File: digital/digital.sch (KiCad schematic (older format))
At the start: 0 parts

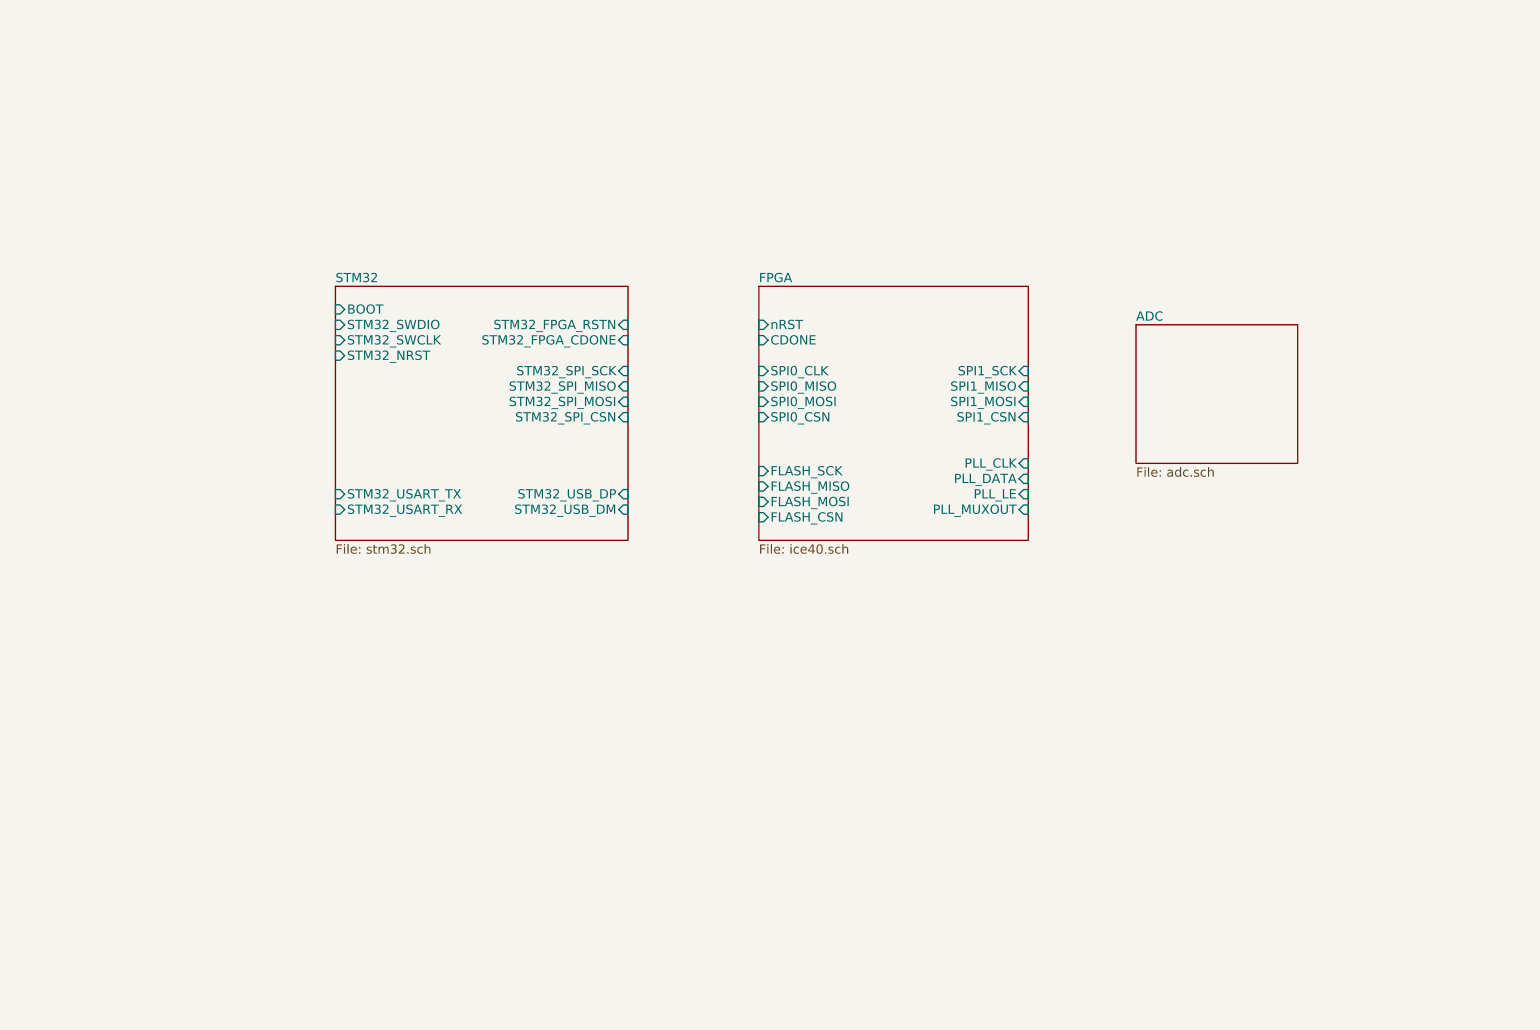
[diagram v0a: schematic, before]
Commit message: Finish schematic TODO footprints
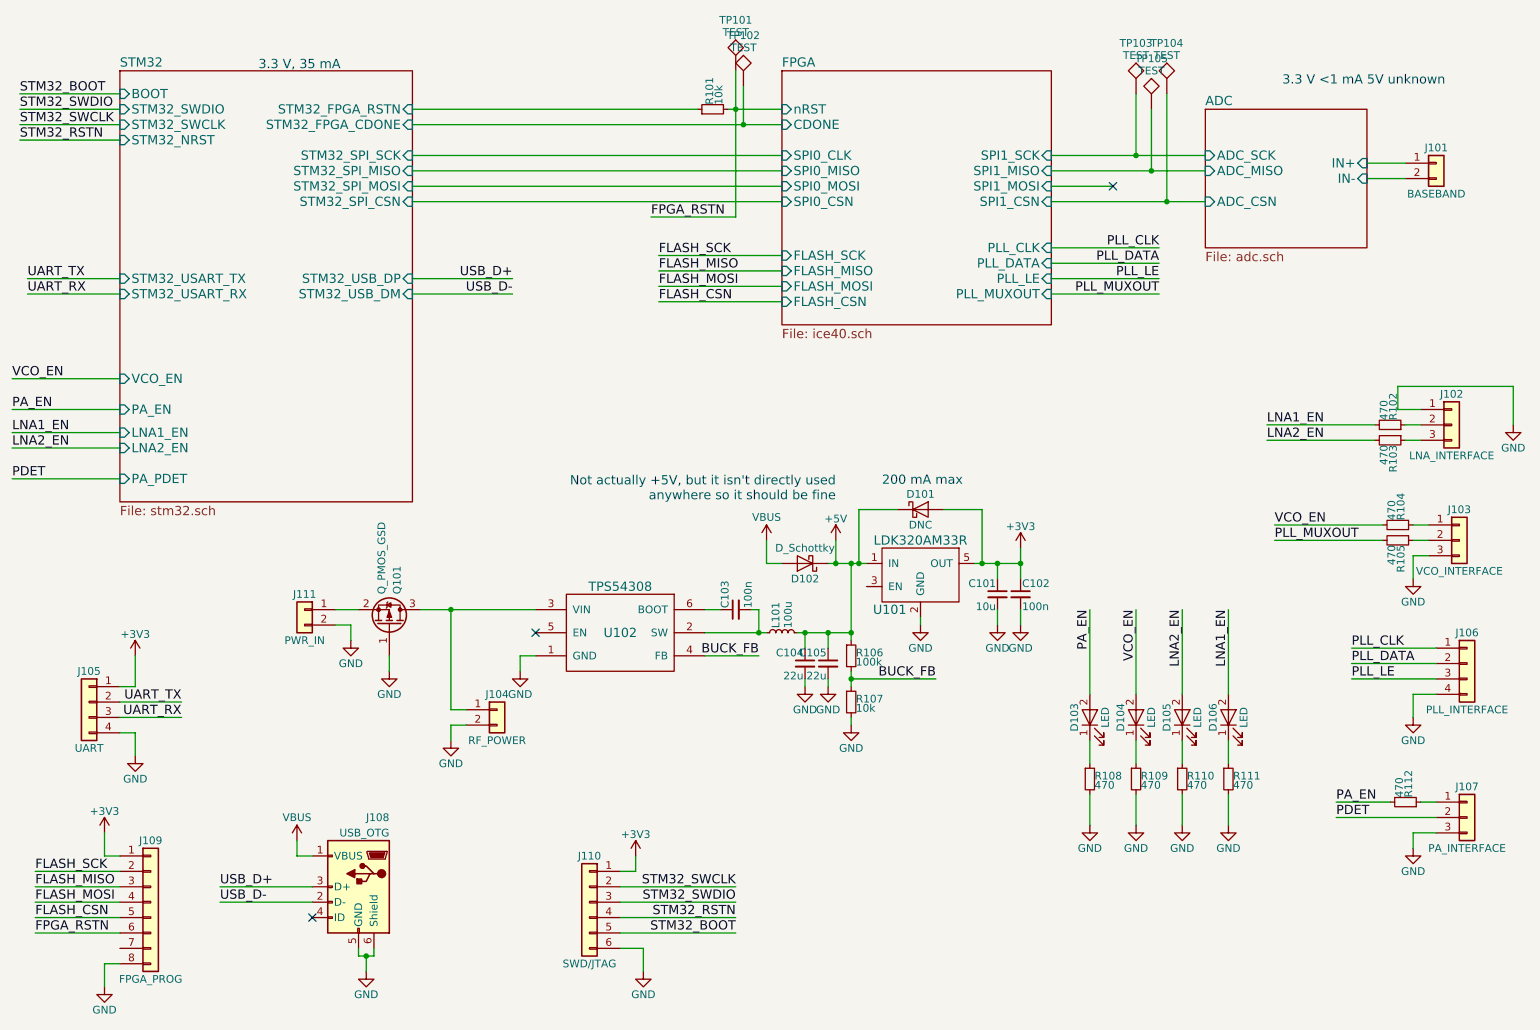
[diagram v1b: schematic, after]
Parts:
- added C101: 10u, symbol C_Small
- added C102, C103: 100n, symbol C_Small
- added C104, C105: 22u, symbol C_Small
- added D101: DNC, symbol D_Schottky
- added D102: D_Schottky, symbol D_Schottky
- added D103, D104, D105, D106: LED, symbol LED
- added J101: BASEBAND, Pin_Headers:Pin_Header_Straight_1x02_Pitch2.54mm, symbol Conn_01x02
- added J102: LNA_INTERFACE, Pin_Headers:Pin_Header_Straight_1x03_Pitch2.54mm, symbol Conn_01x03
- added J103: VCO_INTERFACE, Pin_Headers:Pin_Header_Straight_1x03_Pitch2.54mm, symbol Conn_01x03
- added J104: RF_POWER, Pin_Headers:Pin_Header_Straight_1x02_Pitch2.54mm, symbol Conn_01x02
- added J105: UART, Pin_Headers:Pin_Header_Straight_2x02_Pitch2.54mm, symbol Conn_01x04
- added J106: PLL_INTERFACE, Pin_Headers:Pin_Header_Straight_2x02_Pitch2.54mm, symbol Conn_01x04
- added J107: PA_INTERFACE, Pin_Headers:Pin_Header_Straight_1x03_Pitch2.54mm, symbol Conn_01x03
- added J108: USB_OTG, symbol USB_OTG
- added J109: FPGA_PROG, Pin_Headers:Pin_Header_Straight_2x04_Pitch2.54mm, symbol Conn_01x08
- added J110: SWD/JTAG, Pin_Headers:Pin_Header_Straight_2x03_Pitch2.54mm, symbol Conn_01x06
- added J111: PWR_IN, Pin_Headers:Pin_Header_Straight_1x02_Pitch2.54mm, symbol Conn_01x02
- added L101: 100u, symbol L_Small
- added Q101: Q_PMOS_GSD, TO_SOT_Packages_SMD:SOT-23, symbol Q_PMOS_GSD
- added R101, R107: 10k, symbol R_Small
- added R102, R103, R104, R105, R108, R109, R110, R111, R112: 470, symbol R_Small
- added R106: 100k, symbol R_Small
- added TP101, TP102, TP103, TP104, TP105: TEST, Connectors:PINTST, symbol TEST
- added U101: LDK320AM33R, symbol LDK320AM33R
- added U102: TPS54308, symbol TPS54308
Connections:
- net FPGA/CDONE: now also TP102.1
- net STM32/STM32_FPGA_RSTN: now also R101.1
- new net: J103.1 (Pin_1), R104.1
- new net: J103.2 (Pin_2), R105.1
- new net: J107.1 (Pin_1), R112.1
- new net: J102.2 (Pin_2), R102.1
- new net: J102.3 (Pin_3), R103.1
- new net: J104.1 (Pin_1), Q101.3 (D), U102.3 (VIN)
- new net: D103.1 (K), R108.1
- new net: D106.1 (K), R111.1
- new net: D105.1 (K), R110.1
- new net: D104.1 (K), R109.1
- new net: J111.1 (Pin_1), Q101.2 (S)
- new net: C103.2, L101.1, U102.2 (SW)
- new net: C103.1, U102.6 (BOOT)
- new net +3V3: C101.1, C102.1, D101.2 (A), J105.1 (Pin_1), J109.1 (Pin_1), J110.1 (Pin_1), U101.5 (OUT)
- new net +5V: C104.1, C105.1, D101.1 (K), D102.1 (K), L101.2, R106.1, U101.1 (IN)
- new net ADC/ADC_CSN: TP104.1
- new net ADC/ADC_MISO: TP105.1
- new net ADC/ADC_SCK: TP103.1
- new net ADC/IN+: J101.1 (Pin_1)
- new net ADC/IN-: J101.2 (Pin_2)
- new net BUCK_FB: R106.2, R107.1, U102.4 (FB)
- new net FLASH_CSN: J109.5 (Pin_5)
- new net FLASH_MISO: J109.3 (Pin_3)
- new net FLASH_MOSI: J109.4 (Pin_4)
- new net FLASH_SCK: J109.2 (Pin_2)
- new net FPGA_RSTN: J109.6 (Pin_6), R101.2, TP101.1
- new net GND: C101.2, C102.2, C104.2, C105.2, J102.1 (Pin_1), J103.3 (Pin_3), J104.2 (Pin_2), J105.4 (Pin_4), J106.4 (Pin_4), J107.3 (Pin_3), J108.5 (GND), J108.6 (Shield), J109.8 (Pin_8), J110.6 (Pin_6), J111.2 (Pin_2), Q101.1 (G), R107.2, R108.2, R109.2, R110.2, R111.2, U101.2 (GND), U102.1 (GND)
- new net LNA1_EN: D106.2 (A), R102.2
- new net LNA2_EN: D105.2 (A), R103.2
- new net PA_EN: D103.2 (A), R112.2
- new net PDET: J107.2 (Pin_2)
- new net PLL_CLK: J106.1 (Pin_1)
- new net PLL_DATA: J106.2 (Pin_2)
- new net PLL_LE: J106.3 (Pin_3)
- new net PLL_MUXOUT: R105.2
- new net STM32_BOOT: J110.5 (Pin_5)
- new net STM32_RSTN: J110.4 (Pin_4)
- new net STM32_SWCLK: J110.2 (Pin_2)
- new net STM32_SWDIO: J110.3 (Pin_3)
- new net UART_RX: J105.3 (Pin_3)
- new net UART_TX: J105.2 (Pin_2)
- new net USB_D+: J108.3 (D+)
- new net USB_D-: J108.2 (D-)
- new net VBUS: D102.2 (A), J108.1 (VBUS)
- new net VCO_EN: D104.2 (A), R104.2
- no-connect marks 0 -> 3
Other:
- note added: "200 mA max"
- note added: "3.3 V <1 mA 5V unknown"
- note added: "3.3 V, 35 mA"
- note added: "Not actually +5V, but it isn't directly used\nanywhere so it should be fine"

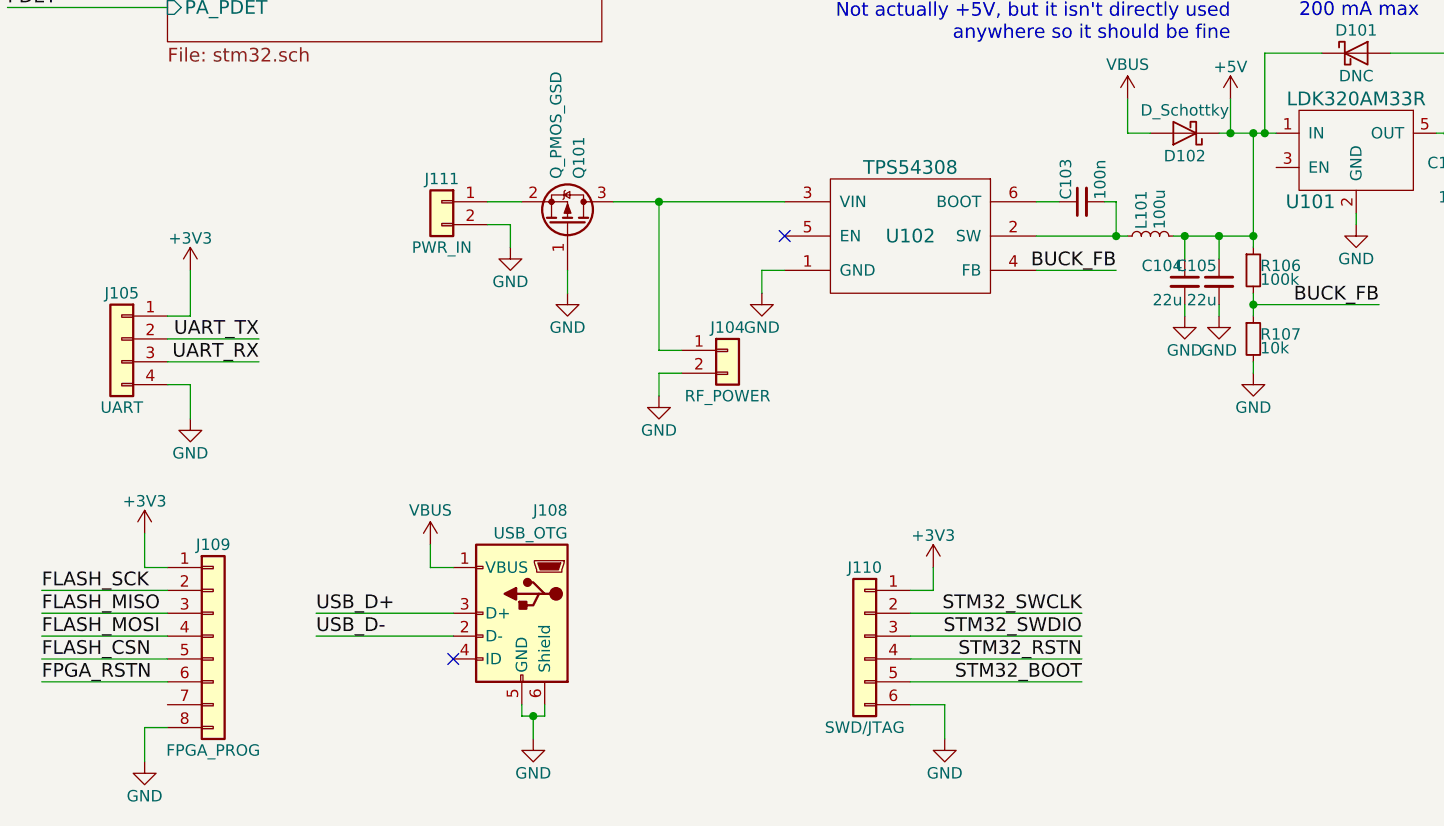
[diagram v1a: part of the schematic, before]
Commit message: Finish schematic and footprinting of digital board
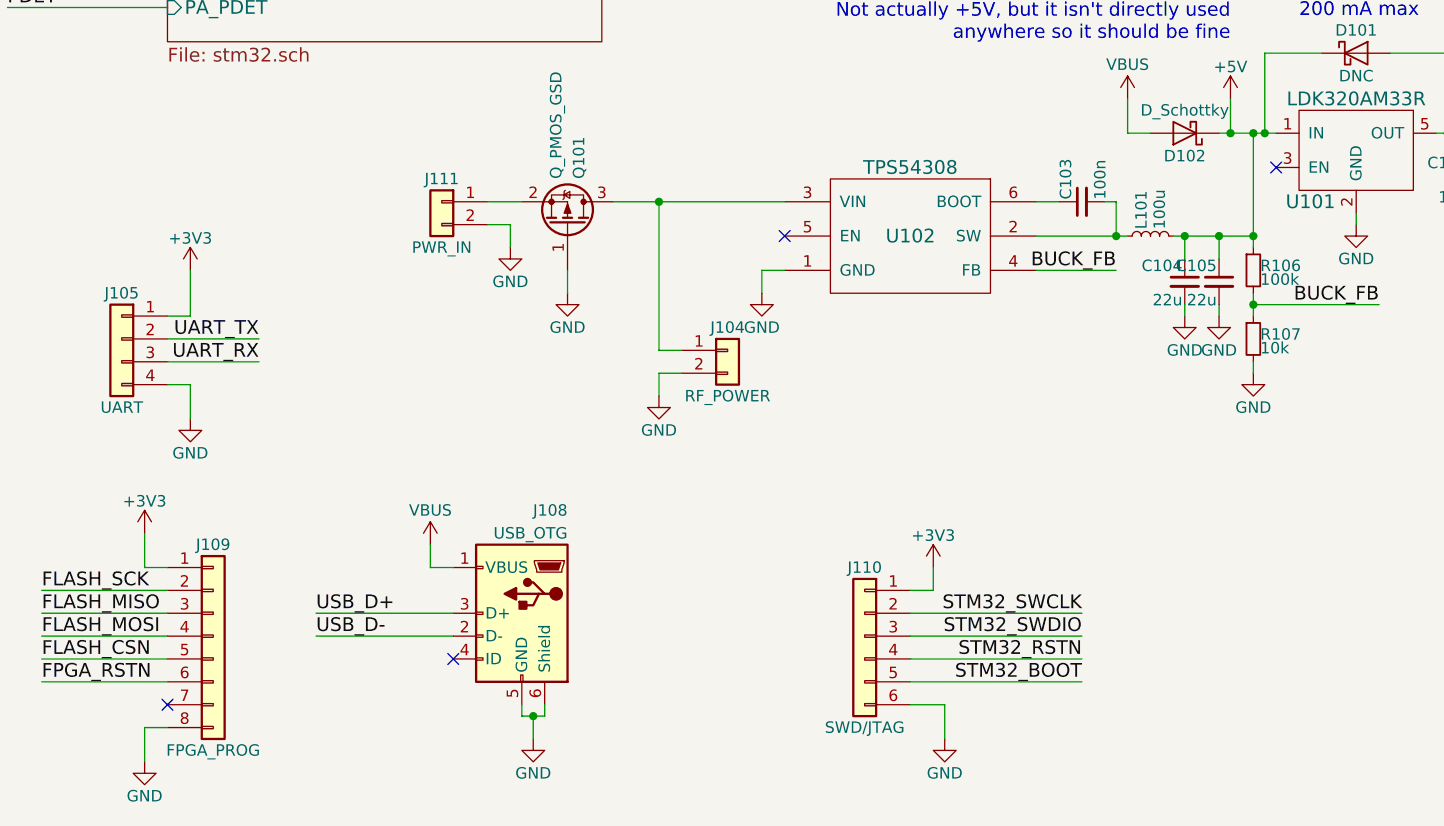
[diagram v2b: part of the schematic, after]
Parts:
- C101: footprint (none) -> Capacitors_SMD:C_0805_HandSoldering
- C102, C103: footprint (none) -> Capacitors_SMD:C_0603_HandSoldering
- C104, C105: footprint (none) -> Capacitors_SMD:C_1210_HandSoldering
- D101, D102: footprint (none) -> digital:Panasonic_Diode-1006
- D103, D104, D105, D106: footprint (none) -> Diodes_SMD:D_0603
- J108: footprint (none) -> digital:10118194
- L101: footprint (none) -> digital:Murata_DG6050C
- R101, R102, R103, R104, R105, R107, R108, R109, R110, R111, R112: footprint (none) -> Resistors_SMD:R_0603_HandSoldering
- R106: footprint (none) -> Resistors_SMD:R_0402
- U101: footprint (none) -> digital:ST_SOT23-5L
- U102: footprint (none) -> digital:TI-SOT-23-6
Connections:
- no-connect marks 3 -> 5

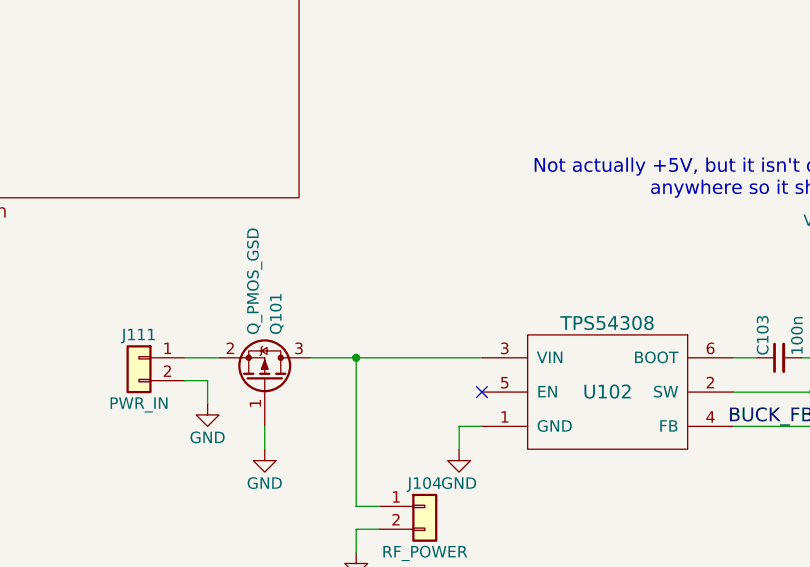
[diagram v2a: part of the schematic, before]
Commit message: Add gain stage; hopefully ready to start layout now
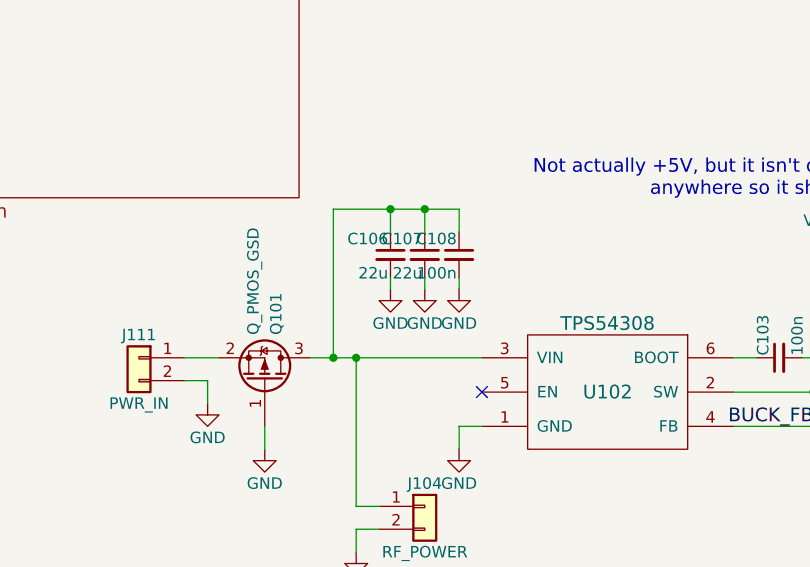
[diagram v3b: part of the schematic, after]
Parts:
- added C106, C107: 22u, Capacitors_SMD:C_1210_HandSoldering, symbol C_Small
- added C108: 100n, Capacitors_SMD:C_0603_HandSoldering, symbol C_Small
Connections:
- net GND: now also C106.2, C107.2, C108.2
- net at J104.1 (Pin_1), Q101.3 (D), U102.3 (VIN): now also C106.1, C107.1, C108.1
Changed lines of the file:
@@
 LIBS:ldk320am33r
 LIBS:tlv74125pdbvr
+LIBS:opa2376qdgkrq1
 LIBS:digital-cache
 EELAYER 25 0
@@
 NoConn ~ 6400 4300
 NoConn ~ 1550 6650
+$Comp
+L C_Small C107
+U 1 1 5AD67393
+P 4000 4000
+F 0 "C107" H 4010 4070 50  0000 L CNN
+F 1 "22u" H 4010 3920 50  0000 L CNN
+F 2 "Capacitors_SMD:C_1210_HandSoldering" H 4000 4000 50  0001 C CNN
+F 3 "" H 4000 4000 50  0001 C CNN
+	1    4000 4000
+	-1   0    0    -1
+$EndComp
+$Comp
+L C_Small C108
+U 1 1 5AD67554
+P 4150 4000
+F 0 "C108" H 4160 4070 50  0000 L CNN
+F 1 "100n" H 4160 3920 50  0000 L CNN
+F 2 "Capacitors_SMD:C_0603_HandSoldering" H 4150 4000 50  0001 C CNN
+F 3 "" H 4150 4000 50  0001 C CNN
+	1    4150 4000
+	-1   0    0    -1
+$EndComp
+Wire Wire Line
+	3600 4450 3600 3800
+Wire Wire Line
+	3600 3800 4150 3800
+Wire Wire Line
+	3850 3800 3850 3900
+Connection ~ 3600 4450
+Wire Wire Line
+	4000 3800 4000 3900
+Connection ~ 3850 3800
+$Comp
+L GND #PWR030
+U 1 1 5AD67F9A
+P 4000 4150
+F 0 "#PWR030" H 4000 3900 50  0001 C CNN
+F 1 "GND" H 4000 4000 50  0000 C CNN
+F 2 "" H 4000 4150 50  0001 C CNN
+F 3 "" H 4000 4150 50  0001 C CNN
+	1    4000 4150
+	1    0    0    -1
+$EndComp
+$Comp
+L GND #PWR031
+U 1 1 5AD68128
+P 4150 4150
+F 0 "#PWR031" H 4150 3900 50  0001 C CNN
+F 1 "GND" H 4150 4000 50  0000 C CNN
+F 2 "" H 4150 4150 50  0001 C CNN
+F 3 "" H 4150 4150 50  0001 C CNN
+	1    4150 4150
+	1    0    0    -1
+$EndComp
+Wire Wire Line
+	4150 4100 4150 4150
+Wire Wire Line
+	4000 4100 4000 4150
+$Comp
+L C_Small C106
+U 1 1 5AD692CA
+P 3850 4000
+F 0 "C106" H 3860 4070 50  0000 L CNN
+F 1 "22u" H 3860 3920 50  0000 L CNN
+F 2 "Capacitors_SMD:C_1210_HandSoldering" H 3850 4000 50  0001 C CNN
+F 3 "" H 3850 4000 50  0001 C CNN
+	1    3850 4000
+	-1   0    0    -1
+$EndComp
+$Comp
+L GND #PWR032
+U 1 1 5AD69462
+P 3850 4150
+F 0 "#PWR032" H 3850 3900 50  0001 C CNN
+F 1 "GND" H 3850 4000 50  0000 C CNN
+F 2 "" H 3850 4150 50  0001 C CNN
+F 3 "" H 3850 4150 50  0001 C CNN
+	1    3850 4150
+	1    0    0    -1
+$EndComp
+Wire Wire Line
+	3850 4100 3850 4150
+Wire Wire Line
+	4150 3800 4150 3900
+Connection ~ 4000 3800
 $EndSCHEMATC

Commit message: Line up connectors across both boards, spread out component footprints
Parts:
- J106: footprint Pin_Headers:Pin_Header_Straight_2x02_Pitch2.54mm -> Pin_Headers:Pin_Header_Straight_1x04_Pitch2.54mm
- TP101, TP102, TP103, TP104, TP105: footprint Connectors:PINTST -> SMD_Packages:1Pin
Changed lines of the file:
@@
 F 0 "TP101" H 5550 1250 50  0000 C BNN
 F 1 "TEST" H 5550 1200 50  0000 C CNN
-F 2 "Connectors:PINTST" H 5550 950 50  0001 C CNN
+F 2 "SMD_Packages:1Pin" H 5550 950 50  0001 C CNN
 F 3 "" H 5550 950 50  0001 C CNN
 	1    5550 950
@@
 F 0 "TP102" H 5600 1350 50  0000 C BNN
 F 1 "TEST" H 5600 1300 50  0000 C CNN
-F 2 "Connectors:PINTST" H 5600 1050 50  0001 C CNN
+F 2 "SMD_Packages:1Pin" H 5600 1050 50  0001 C CNN
 F 3 "" H 5600 1050 50  0001 C CNN
 	1    5600 1050
@@
 F 0 "J106" H 10300 5000 50  0000 C CNN
 F 1 "PLL_INTERFACE" H 10300 4500 50  0000 C CNN
-F 2 "Pin_Headers:Pin_Header_Straight_2x02_Pitch2.54mm" H 10300 4800 50  0001 C CNN
+F 2 "Pin_Headers:Pin_Header_Straight_1x04_Pitch2.54mm" H 10300 4800 50  0001 C CNN
 F 3 "" H 10300 4800 50  0001 C CNN
 	1    10300 4800
@@
 F 0 "TP103" H 8150 1400 50  0000 C BNN
 F 1 "TEST" H 8150 1350 50  0000 C CNN
-F 2 "Connectors:PINTST" H 8150 1100 50  0001 C CNN
+F 2 "SMD_Packages:1Pin" H 8150 1100 50  0001 C CNN
 F 3 "" H 8150 1100 50  0001 C CNN
 	1    8150 1100
@@
 F 0 "TP105" H 8250 1500 50  0000 C BNN
 F 1 "TEST" H 8250 1450 50  0000 C CNN
-F 2 "Connectors:PINTST" H 8250 1200 50  0001 C CNN
+F 2 "SMD_Packages:1Pin" H 8250 1200 50  0001 C CNN
 F 3 "" H 8250 1200 50  0001 C CNN
 	1    8250 1200
@@
 F 0 "TP104" H 8350 1400 50  0000 C BNN
 F 1 "TEST" H 8350 1350 50  0000 C CNN
-F 2 "Connectors:PINTST" H 8350 1100 50  0001 C CNN
+F 2 "SMD_Packages:1Pin" H 8350 1100 50  0001 C CNN
 F 3 "" H 8350 1100 50  0001 C CNN
 	1    8350 1100
